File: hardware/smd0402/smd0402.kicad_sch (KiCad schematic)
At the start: 41 parts, among them J1 Conn_01x03, J2 SAO v1.69bis addon, J3 SAO v1.69bis badge, P1 Conn_01x02, P2 Conn_01x02, P3 Conn_01x02, P4 Conn_01x02, P5 Conn_01x02, P6 Conn_01x02, U1 WCH CH32V003F4U6

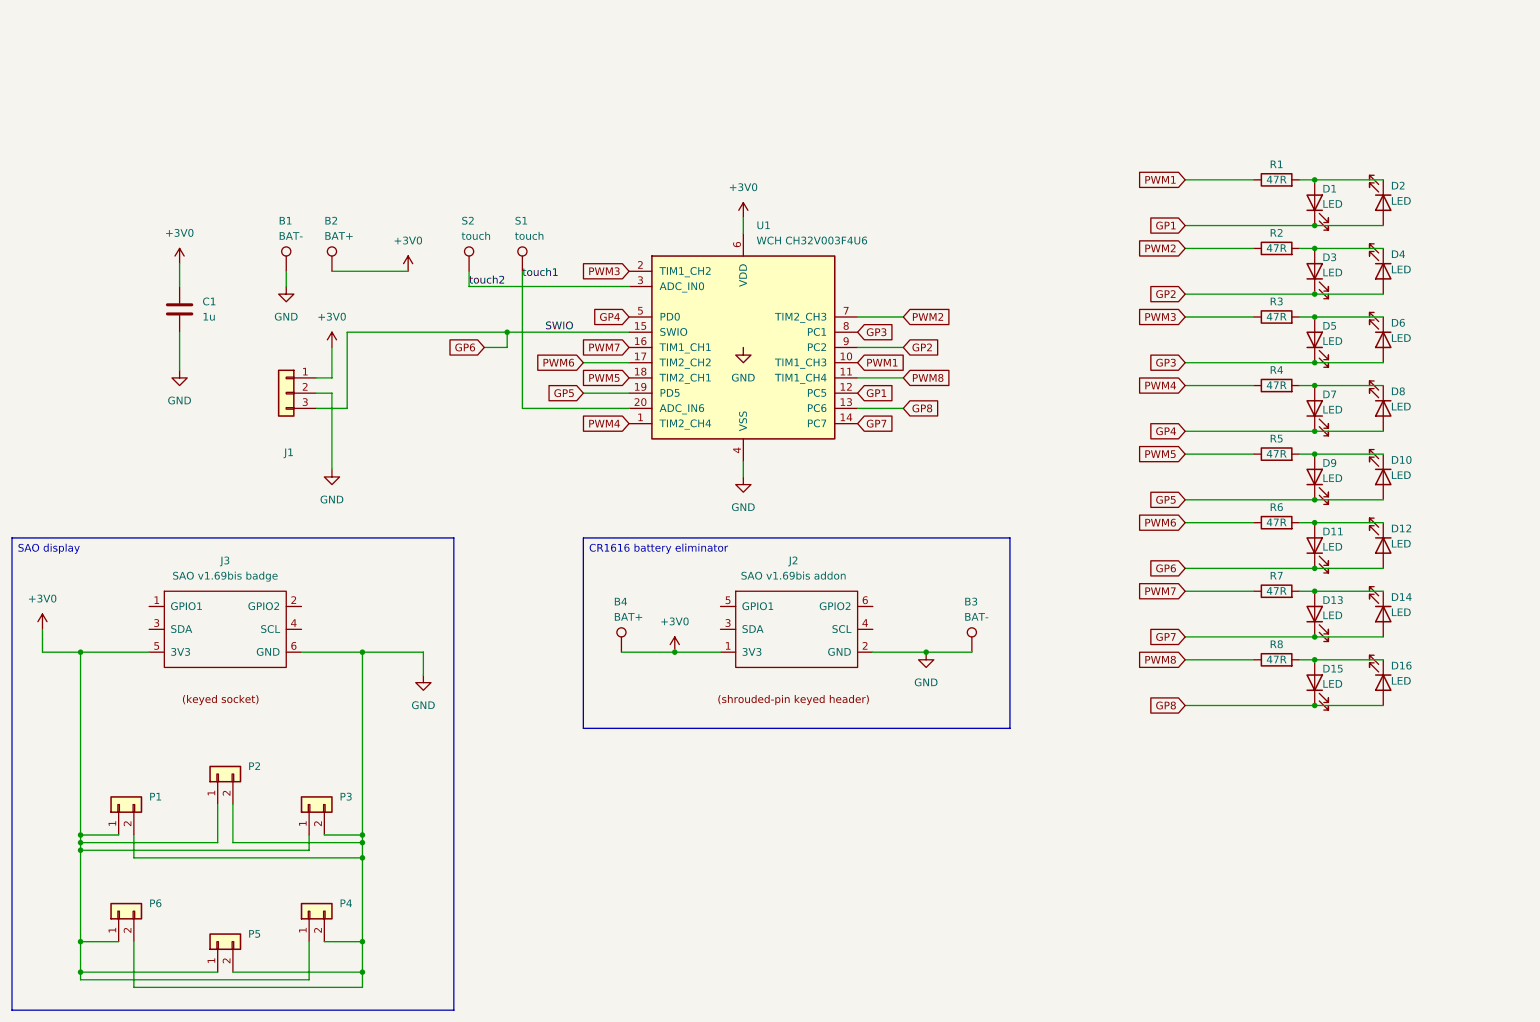
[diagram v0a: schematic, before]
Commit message: added power bypass caps
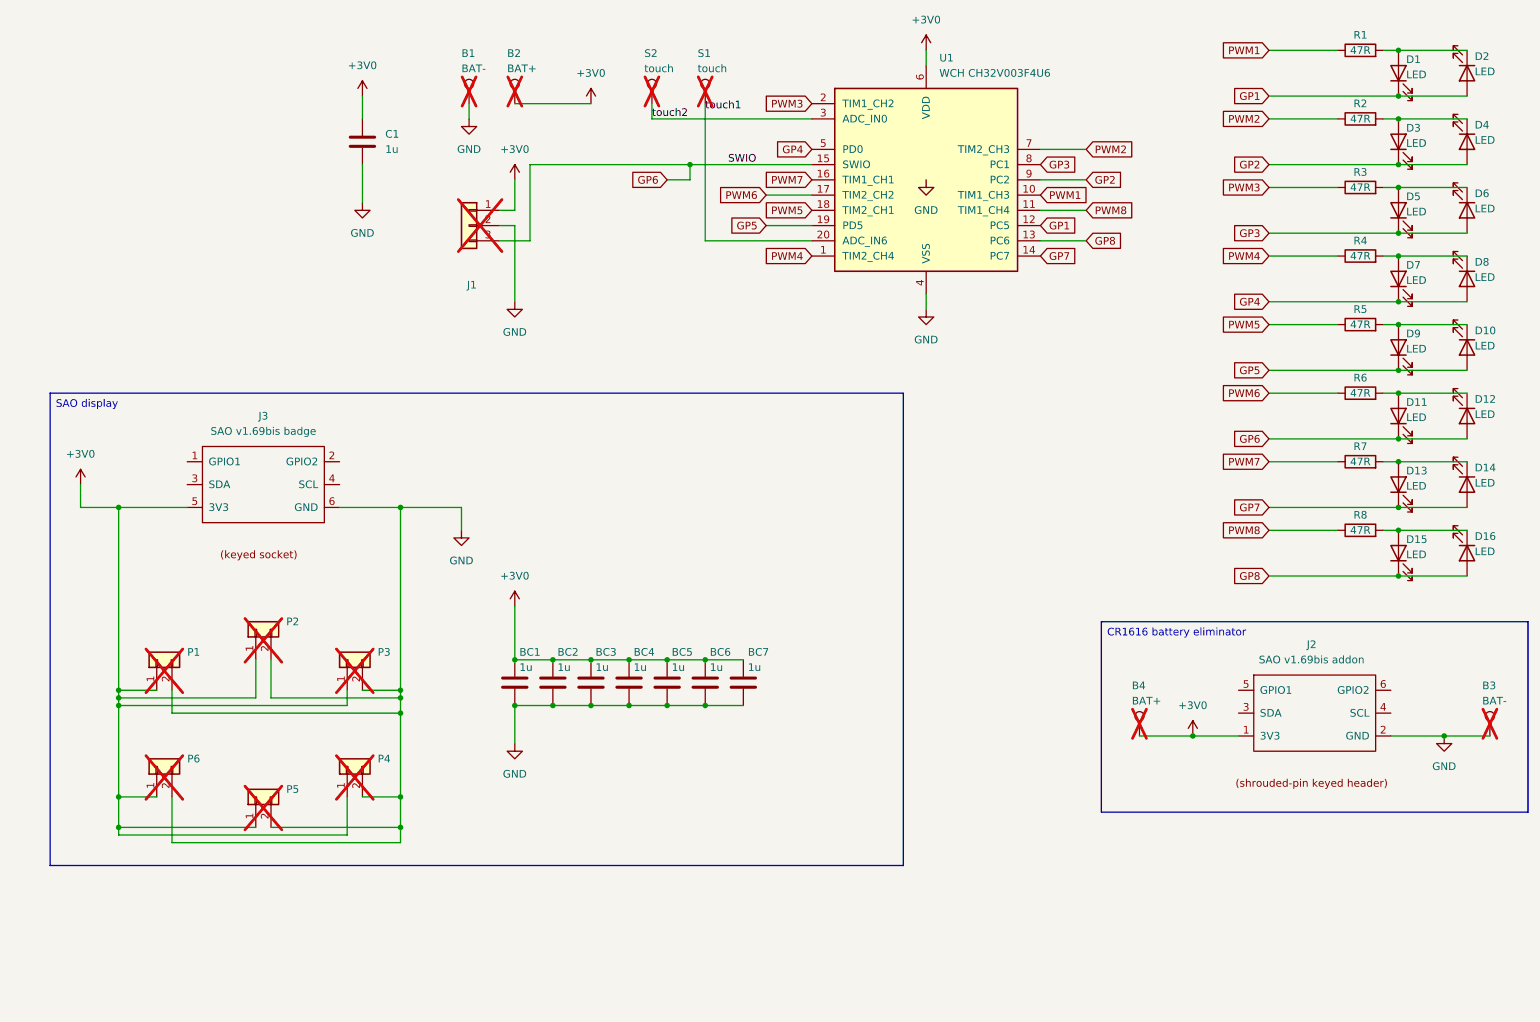
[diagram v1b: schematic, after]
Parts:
- added BC1, BC2, BC3, BC4, BC5, BC6, BC7: 1u, Capacitor_SMD:C_0805_2012Metric_Pad1.18x1.45mm_HandSolder, symbol Device:C
- B1, B2, B3, B4, J1, S1, S2: now not fitted
- P1, P2, P3, P4, P5, P6: now not fitted; now left out of the parts list
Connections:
- net +3V0: now also BC1.1, BC2.1, BC3.1, BC4.1, BC5.1, BC6.1, BC7.1
- net GND: now also BC1.2, BC2.2, BC3.2, BC4.2, BC5.2, BC6.2, BC7.2
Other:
- moved on the sheet: C1, D1, D10, D11, D12, D13, D14, D15, D16, D2, D3, D4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

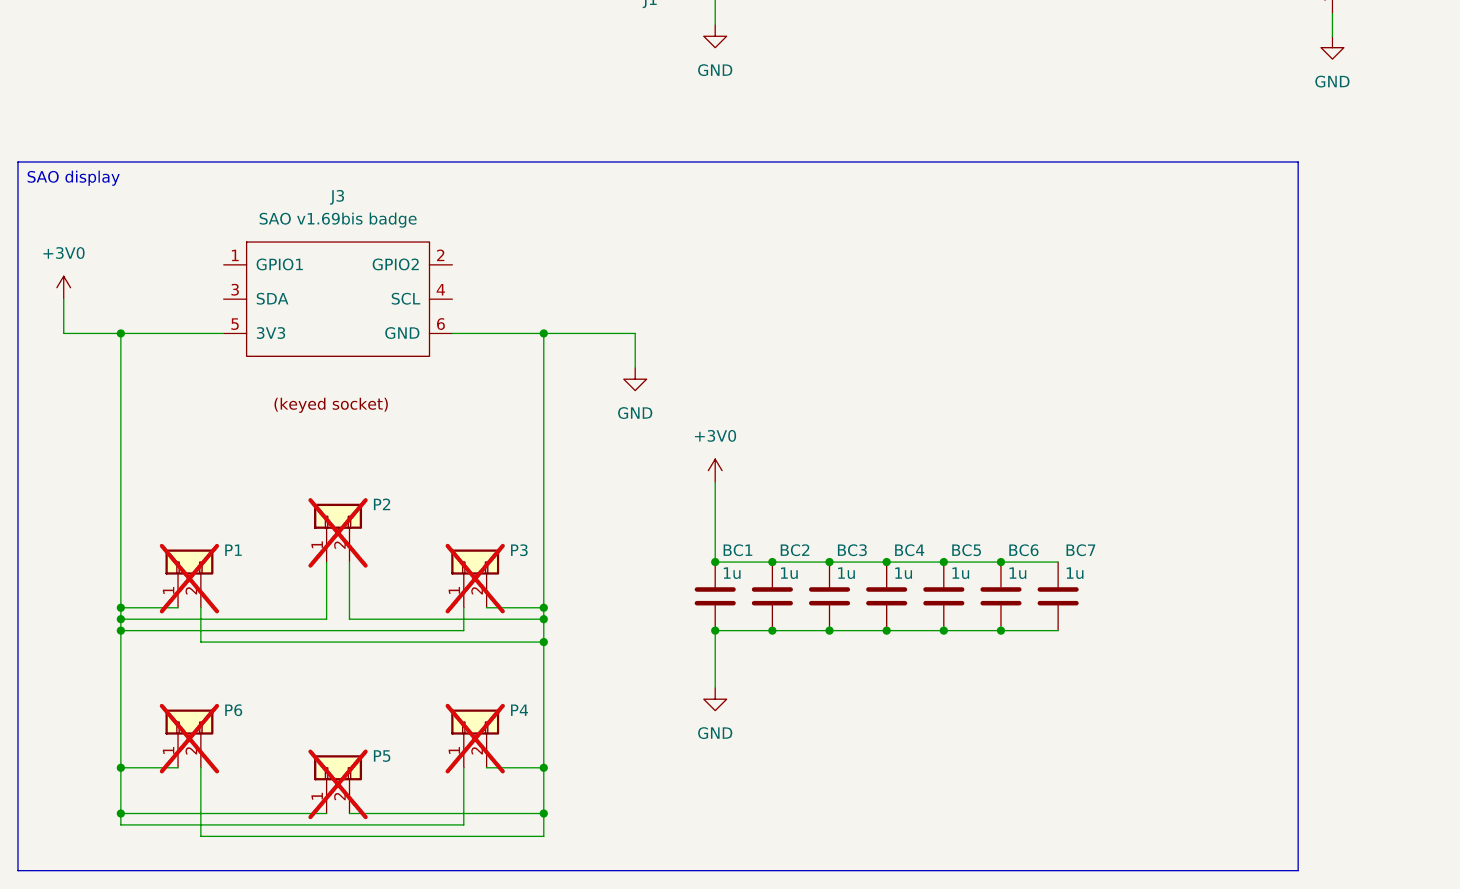
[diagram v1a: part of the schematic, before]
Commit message: remove SAO display
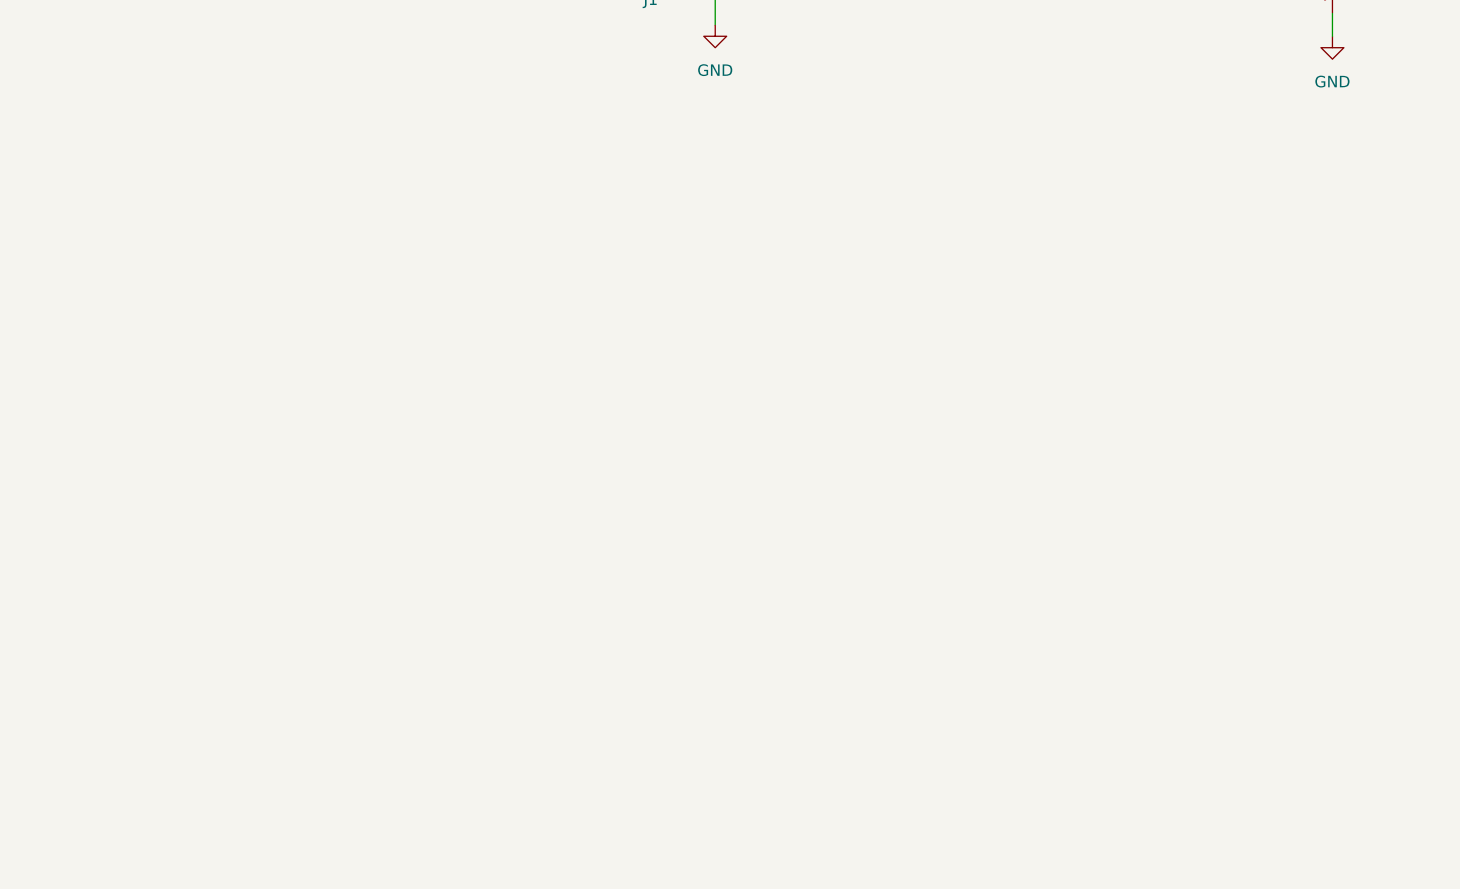
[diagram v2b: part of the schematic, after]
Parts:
- removed BC1, BC2, BC3, BC4, BC5, BC6, BC7: 1u, Capacitor_SMD:C_0805_2012Metric_Pad1.18x1.45mm_HandSolder, symbol Device:C
- removed J3: SAO v1.69bis badge, Connector_IDC:IDC-Header_2x03_P2.54mm_Vertical, symbol extra:SAO v1.69bis badge
- removed P1, P2, P3, P4, P5, P6: Conn_01x02, Connector_PinHeader_2.54mm:PinHeader_1x02_P2.54mm_Vertical, symbol Connector_Generic:Conn_01x02

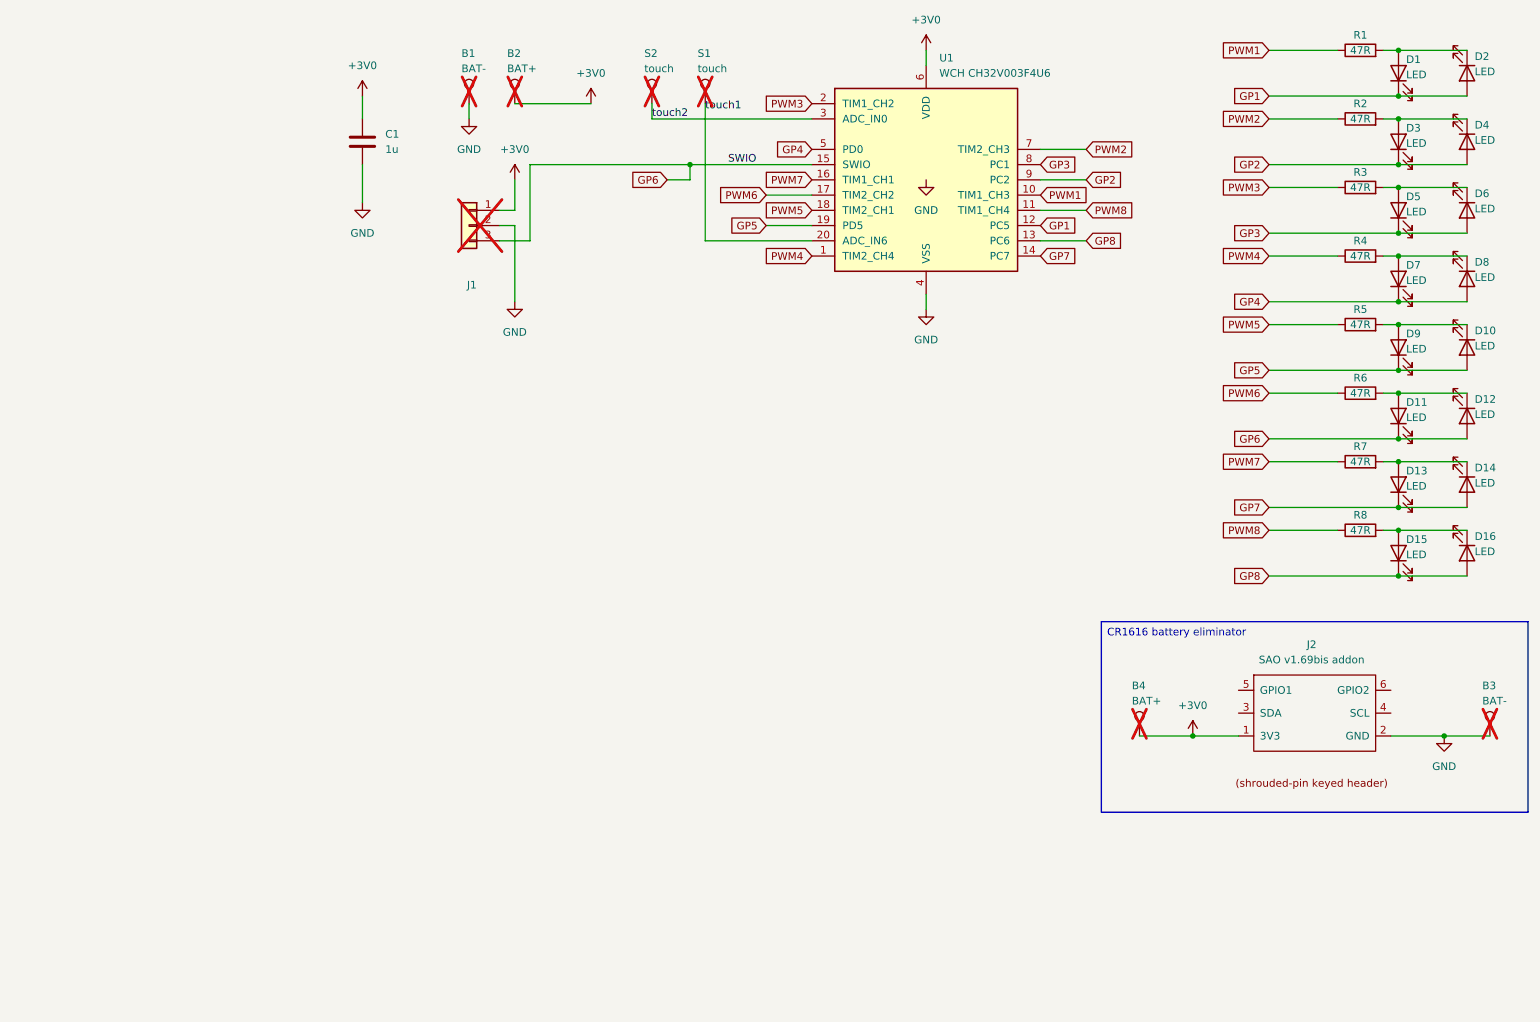
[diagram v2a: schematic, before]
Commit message: update parts to those in stock at JLC *now*
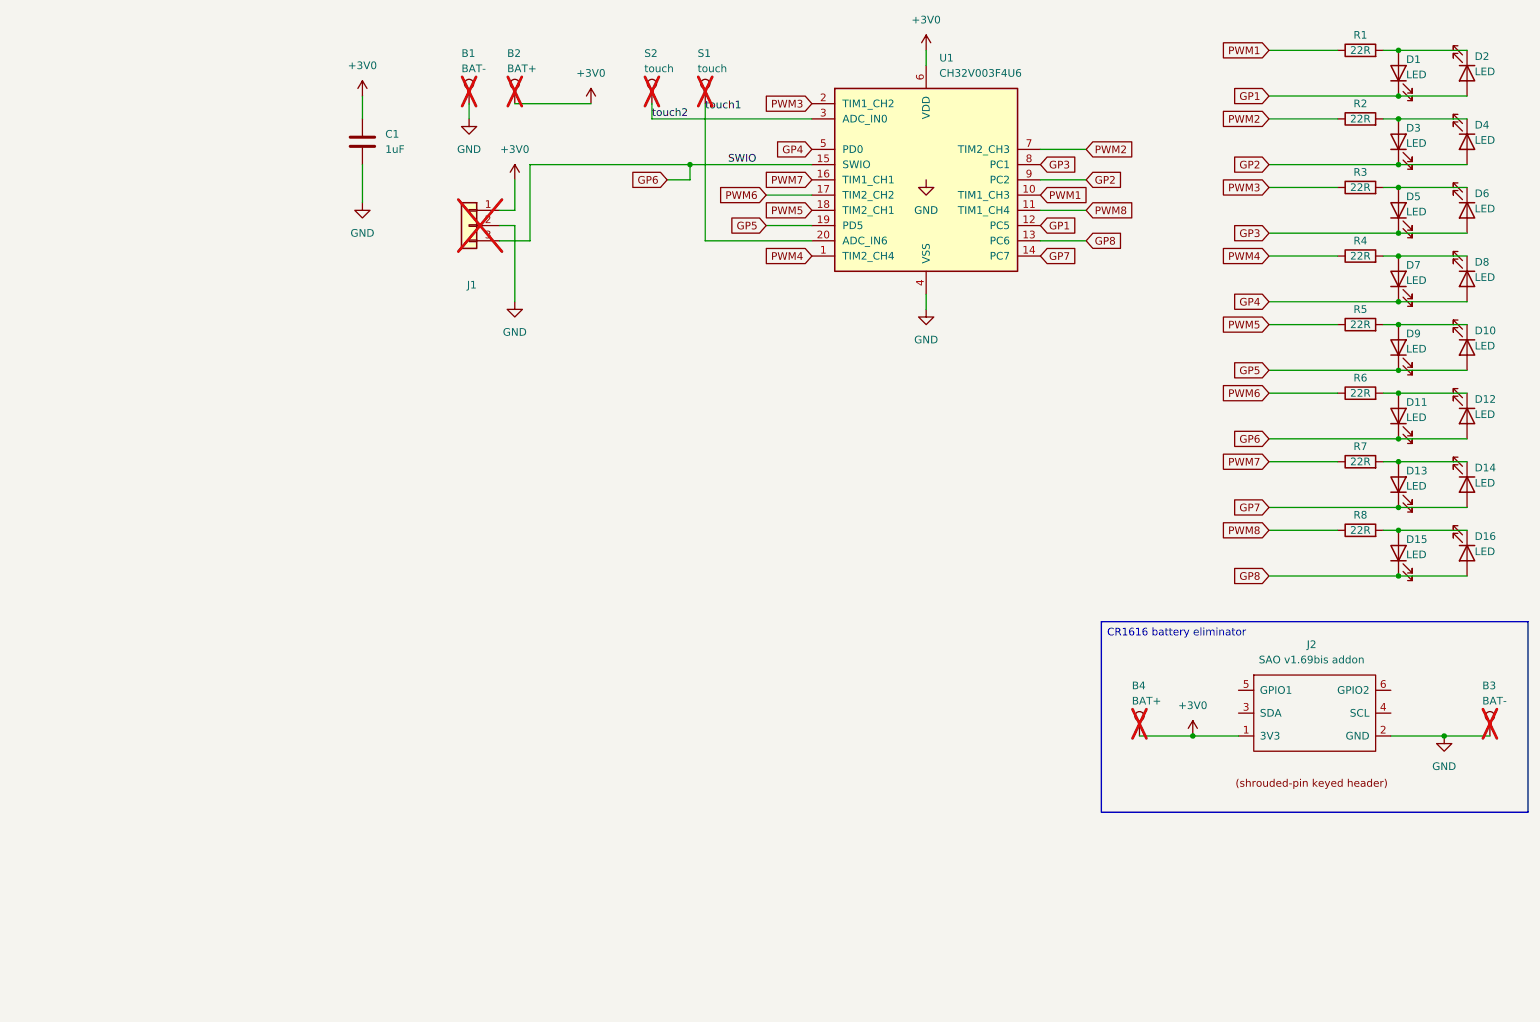
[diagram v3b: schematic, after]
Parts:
- C1: value 1u -> 1uF; JLC (none) -> C25092; LCSC C7393851 -> (none)
- R1, R2, R3, R4, R5, R6, R7, R8: value 47R -> 22R; JLC (none) -> C7496803; LCSC C2909362 -> (none)
- U1: value WCH CH32V003F4U6 -> CH32V003F4U6; JLC (none) -> C5299908
